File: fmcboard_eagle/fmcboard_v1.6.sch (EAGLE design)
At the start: 235 parts, among them IC1 OPA699ID, IC10 LM358, IC11 7805DT, IC12 SN74AUC2G66DCTR, IC13 SN74AUC2G66DCTR, IC14 SN74AUC2G66DCTR, IC15 SN74AUC2G66DCTR, IC16 DAC7578SPWR, IC17 SN74AUC2G66DCTR, IC18 SN74AUC2G66DCTR, IC19 SN74AUC2G66DCTR, IC2 DAC7578SPWR, IC20 SN74AUC2G66DCTR, IC21 74AUP2GU04GW, IC22 74AUP2GU04GW, IC23 74AUP2GU04GW, IC24 74AUP2GU04GW, IC25 MC7905ACD2TR4G, IC26 AMS1117-1.8, IC29 LM337KVURG3, IC3 LTC6229IMS8E#TRPBF, IC4 OPA695IDR, IC5 LTC6229IMS8E#TRPBF, IC6 OPA695IDR, IC7 OPA699ID, IC8 LM358, IC9 LM358, J1 8pin, J10 4p-2.54, J11 4p-2.54, J12 4p-2.54, J13 4p-2.54, J2 ASP-134604-01, J3 4p-2.54, J4 4p-2.54, J5 4p-2.54, J6 4p-2.54, J7 4p-2.54, J8 4p-2.54, J9 8pin

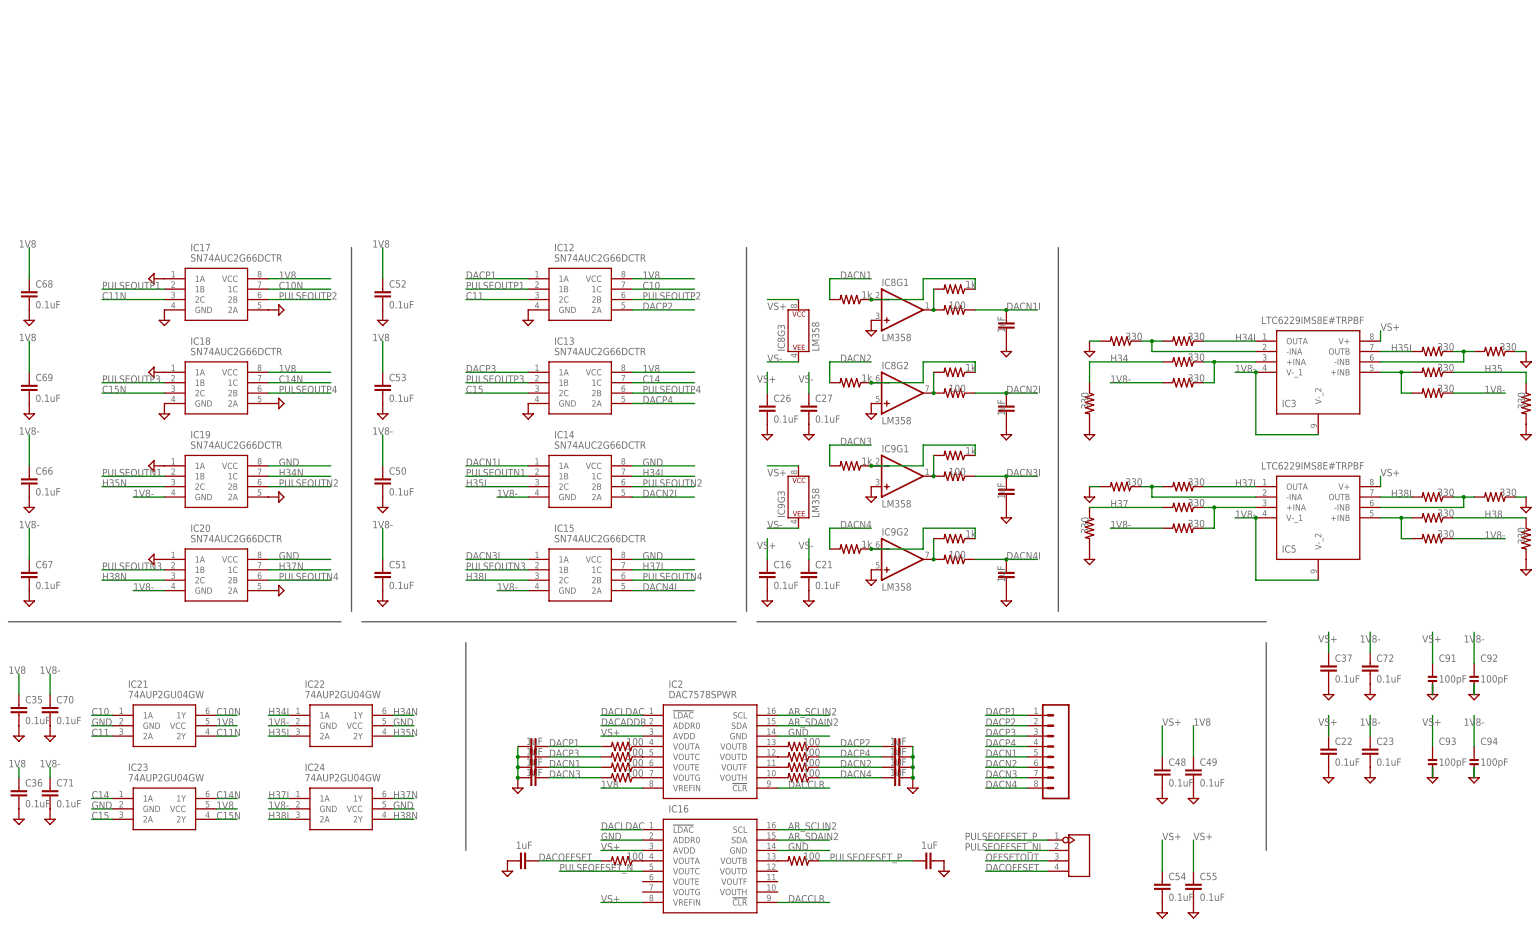
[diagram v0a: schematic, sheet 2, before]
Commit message: Added extra 4 DAC outputs, 2 positive and 2 negative Copies of pulse out and amp out to sma - TODO
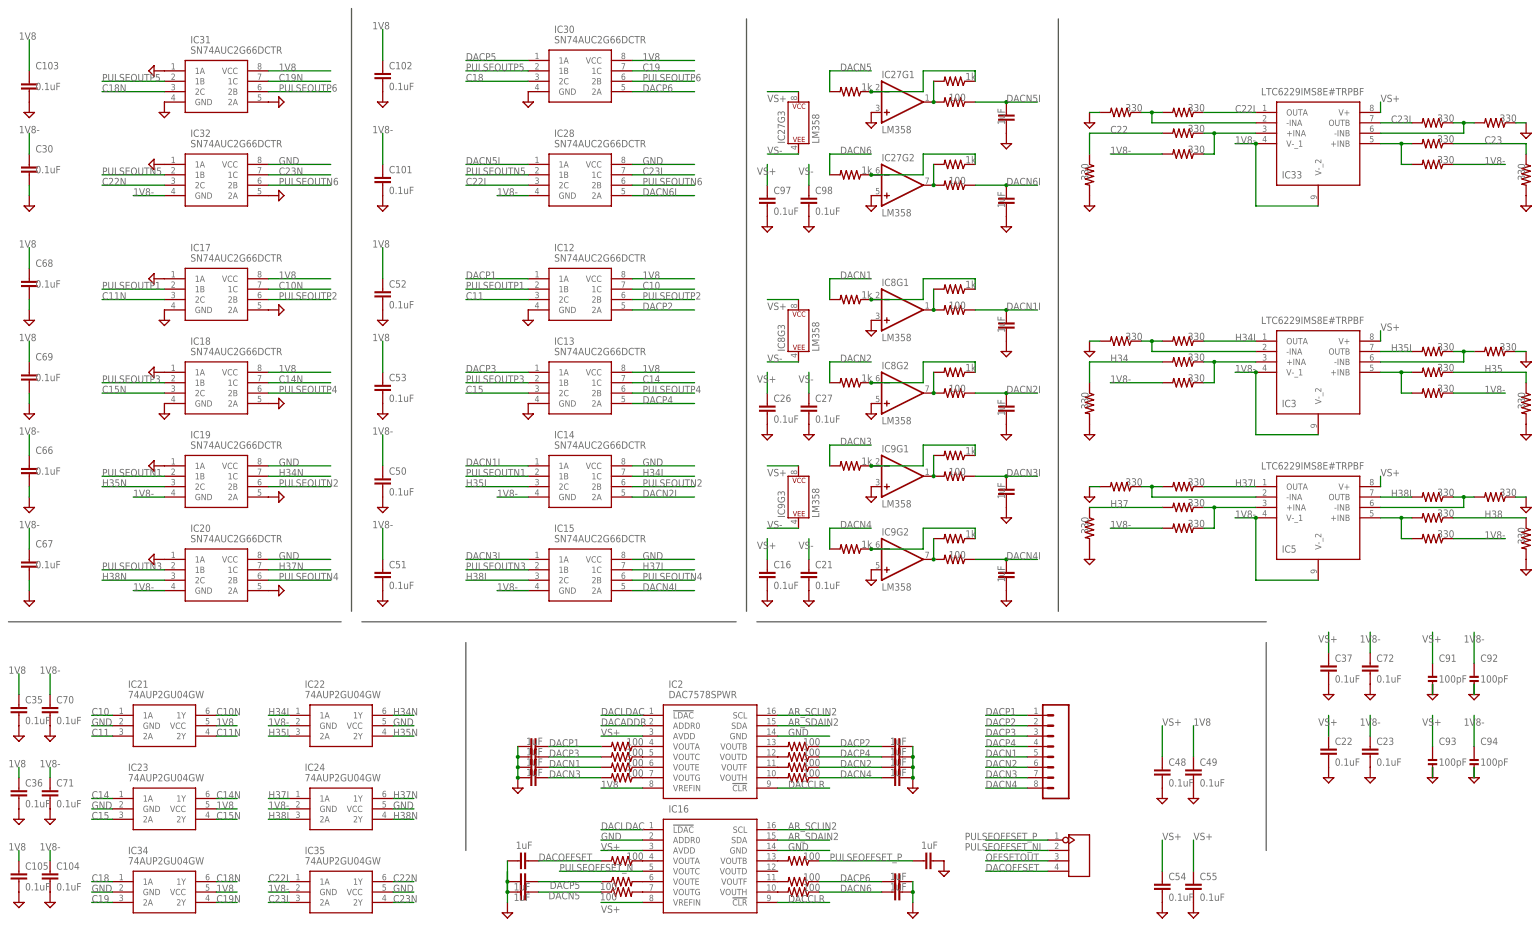
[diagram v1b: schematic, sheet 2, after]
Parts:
- removed J10: 4p-2.54, Seeed-Connector:DIP-BLACK-FEMALE-HEADER-VERT(4P-2.54)
- added C100, C31, C89, C90, C96, C99: 1uF, SparkFun-Passives:CAP0805
- added C101, C102, C104, C105, C97, C98: 0.1uF, SparkFun-Passives:CAP0805
- added C103, C30: 0.1uF, rcl:C-EUC0402K
- added IC27: LM358, SparkFun-IC-Amplifiers:OPAMP-DUALU
- added IC28, IC30, IC31, IC32: SN74AUC2G66DCTR, SN74AUC2G66DCTR:SN74AUC2G66DCTR
- added IC33: LTC6229IMS8E#TRPBF, LTC6229IMS8E#TRPBF:LTC6229IMS8E#TRPBF
- added IC34, IC35: 74AUP2GU04GW, 74AUP2GU04GW_125:74AUP2GU04GW,125
- added R100, R101, R92, R93, R94, R95: 100, rcl:R-US_R0402
- added R102, R103, R104, R105, R106, R107, R108, R109, R110, R91: 330, rcl:R-US_R0402
- added R111, R112, R113, R114: 470, rcl:R-US_R0402
- added R96, R97, R98, R99: 1k, rcl:R-US_R0402
- C66, C67, C68, C69: device SparkFun-Passives:CAP0805 -> rcl:C-EUC0402K
- R1, R10, R11, R12, R13, R14, R17, R18, R19, R2, R20, R21, R22, R23, R24, R25, R26, R27, R28, R29, R3, R30, R31, R32, R33, R34, R35, R36, R37, R38, R39, R40, R41, R42, R43, R44, R45, R46, R47, R48, R49, R50, R51, R52, R53, R54, R55, R56, R57, R58, R59, R6, R60, R61, R62, R63, R64, R65, R66, R67, R68, R69, R7, R70, R73, R74, R75, R76, R77, R78, R79, R8, R80, R81, R82, R83, R84, R85, R87, R88, R90: device rcl:R-US_R0805 -> rcl:R-US_R0402
- R15, R16, R4, R5: device SparkFun-Resistors:RESISTORAXIAL-0.3 -> rcl:R-US_R0402
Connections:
- new net C18N: IC31.2C, IC34.1Y
- new net C19N: IC31.1C, IC34.2Y
- new net C22I: IC28.2C, IC33.OUTA, IC35.1A, R103.1
- new net C22N: IC32.2C, IC35.1Y
- new net C23I: IC28.1C, IC33.OUTB, IC35.2A, R107.2
- new net C23N: IC32.1C, IC35.2Y
- new net DACN5: C96.1, R95.1, R98.2
- new net DACN5I: C99.2, IC28.1A, R100.1
- new net DACN6: C89.1, R93.1, R99.2
- new net DACN6I: C100.2, IC28.2A, R101.1
- new net DACP5: C90.1, IC30.1A, R94.1
- new net DACP6: C31.1, IC30.2A, R92.1
- new net N$1: IC33.-INA, R103.2, R104.1
- new net N$18: IC16.VOUTF, R92.2
- new net N$41: IC16.VOUTH, R93.2
- new net N$43: IC16.VOUTE, R94.2
- new net N$44: IC16.VOUTG, R95.2
- new net N$45: IC27G2.OUT, R101.2, R96.2
- new net N$46: IC27G1.OUT, R100.2, R97.2
- new net N$47: IC27G1.-IN, R97.1, R98.1
- new net N$48: IC27G2.-IN, R96.1, R99.1
- new net N$49: IC33.-INB, R107.1, R108.2
- new net N$50: IC33.+INA, R102.1, R91.1
- new net N$51: IC33.+INB, R105.2, R106.2
- new net PULSEOUTN5: IC28.1B, IC32.1B, R112.2
- new net PULSEOUTN6: IC28.2B, IC32.2B, R114.2
- new net PULSEOUTP5: IC30.1B, IC31.1B, R111.2
- new net PULSEOUTP6: IC30.2B, IC31.2B, R113.2
- net 1V8: now also C102.1, C103.1, C105.1, IC30.VCC, IC31.VCC, IC34.VCC
- net 1V8-: now also C101.1, C104.1, C30.1, IC28.GND, IC32.GND, IC33.V-_1, IC33.V-_2, IC35.GND, R102.2, R106.1
- net C18: now also IC30.2C, IC34.1A; no longer J10.P$1
- net C19: now also IC30.1C, IC34.2A; no longer J10.P$2
- net C22: now also R109.1, R91.2; no longer J10.P$3
- net C23: now also R105.1, R110.1; no longer J10.P$4
- net GND: now also C100.1, C101.2, C102.2, C103.2, C104.2, C105.2, C30.2, C31.2, C89.2, C90.2, C96.2, C97.2, C98.2, C99.1, IC27G1.+IN, IC27G2.+IN, IC28.VCC, IC30.GND, IC31.1A, IC31.2A, IC31.GND, IC32.1A, IC32.2A, IC32.VCC, IC34.GND, IC35.VCC, R104.2, R108.1, R109.2, R110.2
- net PULSESUMIN: now also R111.1, R112.1, R113.1, R114.1
- net VS+: now also C97.1, IC27G3.P$V+, IC33.V+
- net VS-: now also C98.1, IC27G3.P$V-
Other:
- note removed: "extra"
- moved on the sheet: C66, C67, C68, C69

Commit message: Added extra 4 DAC outputs, 2 positive and 2 negative Move to 0402 R and C Copies of pulse out and amp out to sma - TODO
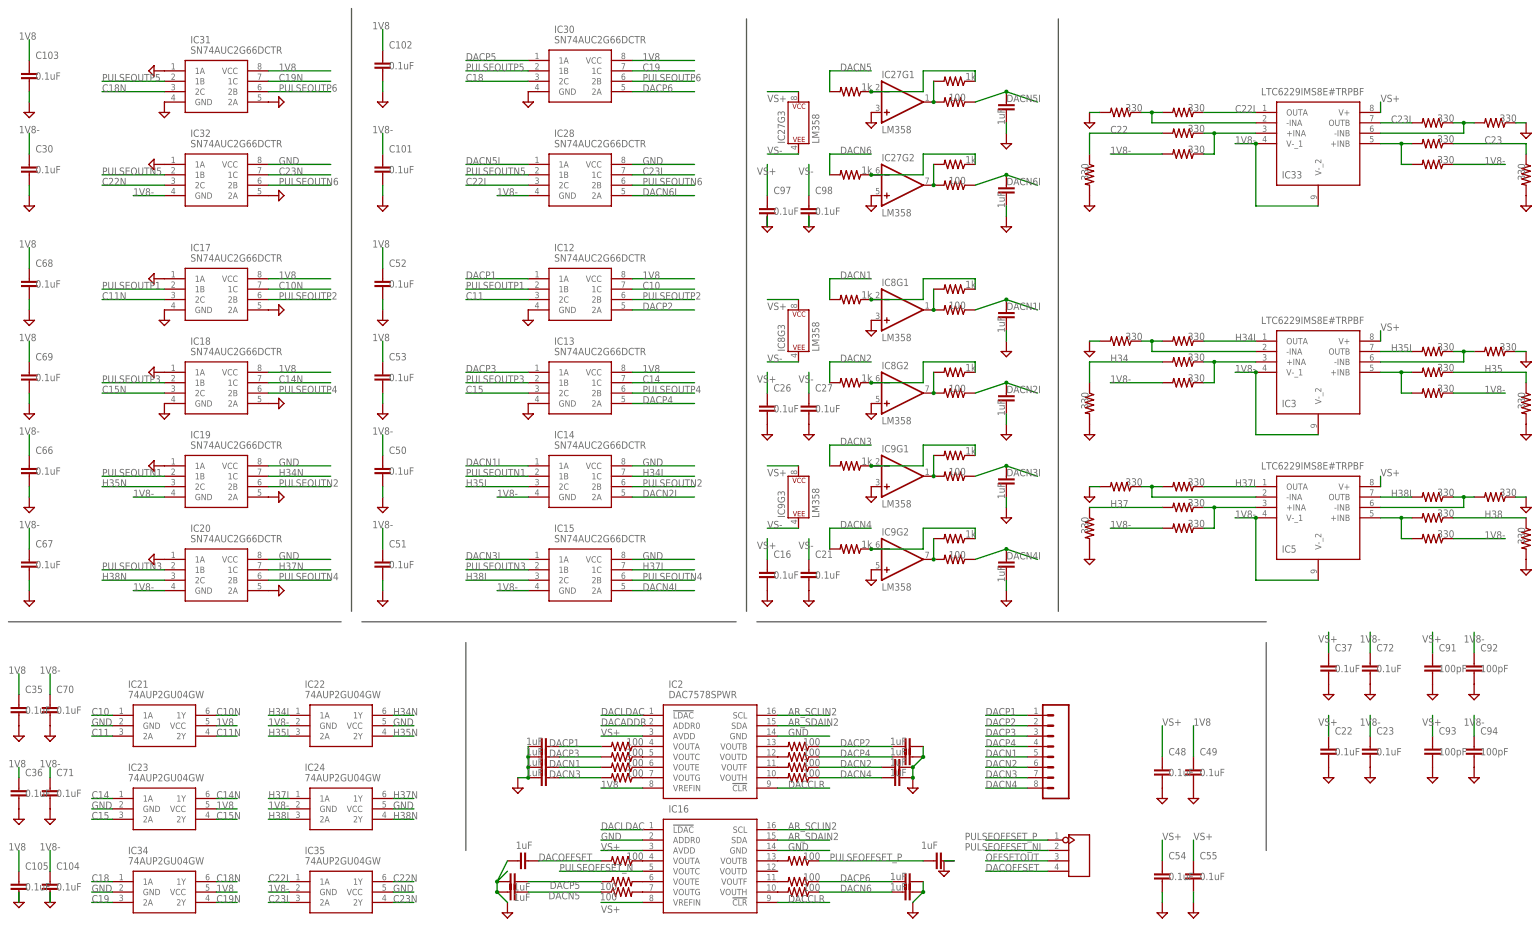
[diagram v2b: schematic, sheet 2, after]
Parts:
- C1, C10, C100, C101, C102, C104, C105, C11, C12, C13, C14, C15, C16, C17, C18, C19, C2, C20, C21, C22, C23, C24, C25, C26, C27, C28, C29, C3, C31, C33, C34, C35, C36, C37, C38, C39, C40, C41, C42, C43, C44, C45, C46, C47, C48, C49, C5, C50, C51, C52, C53, C54, C55, C56, C57, C58, C59, C6, C62, C63, C65, C7, C70, C71, C72, C73, C74, C75, C76, C77, C78, C79, C8, C80, C86, C89, C9, C90, C96, C97, C98, C99: device SparkFun-Passives:CAP0805 -> rcl:C-EUC0402K
- C32, C81, C82, C83, C84, C85, C87, C88, C91, C92, C93, C94: device passives:CAPACITOR0603_CAP -> rcl:C-EUC0402K
- R71, R72, R86, R89: device rcl:R-US_R0805 -> rcl:R-US_R0402
- R9: device SparkFun-Resistors:RESISTORAXIAL-0.3 -> resistor:R-US_R0805
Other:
- moved on the sheet: C101, C102, C103, C104, C105, C50, C51, C52, C53, C54, C55, C97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

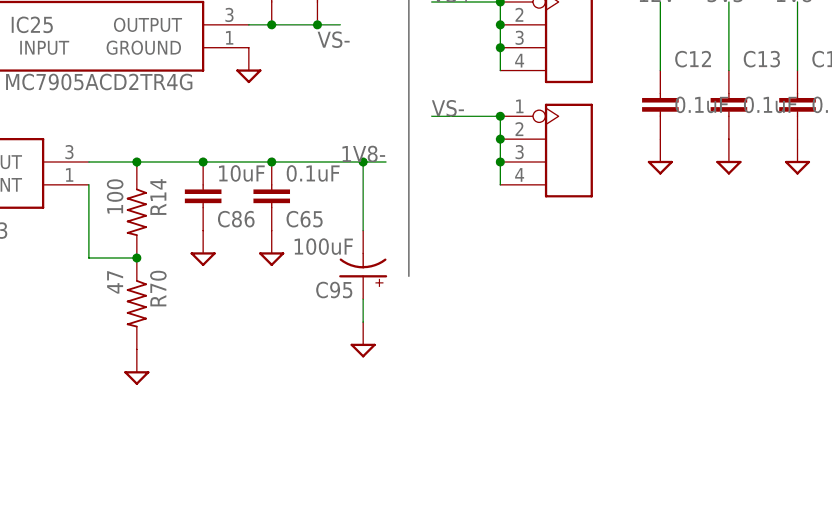
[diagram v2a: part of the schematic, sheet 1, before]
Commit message: Added extra 4 DAC outputs, 2 positive and 2 negative Move all to 0402 R and C Replace 100uF with 10 10uF Copies of pulse out and amp out to sma - TODO
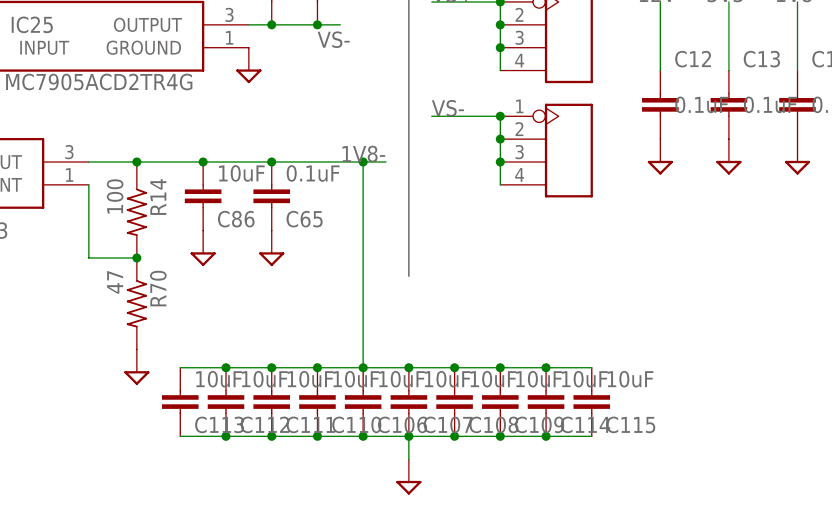
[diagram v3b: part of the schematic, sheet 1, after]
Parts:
- removed C95: 100uF, SparkFun-Passives:CAP_POLSMD
- added C106, C107, C108, C109, C110, C111, C112, C113, C114, C115: 10uF, rcl:C-EUC0402K
- C4, C60, C61, C64: device SparkFun-Passives:CAP0805 -> rcl:C-EUC0402K
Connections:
- net 1V8-: now also C106.1, C107.1, C108.1, C109.1, C110.1, C111.1, C112.1, C113.1, C114.1, C115.1; no longer C95.-
- net GND: now also C106.2, C107.2, C108.2, C109.2, C110.2, C111.2, C112.2, C113.2, C114.2, C115.2; no longer C95.+
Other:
- moved on the sheet: C104, C105, C97, C98

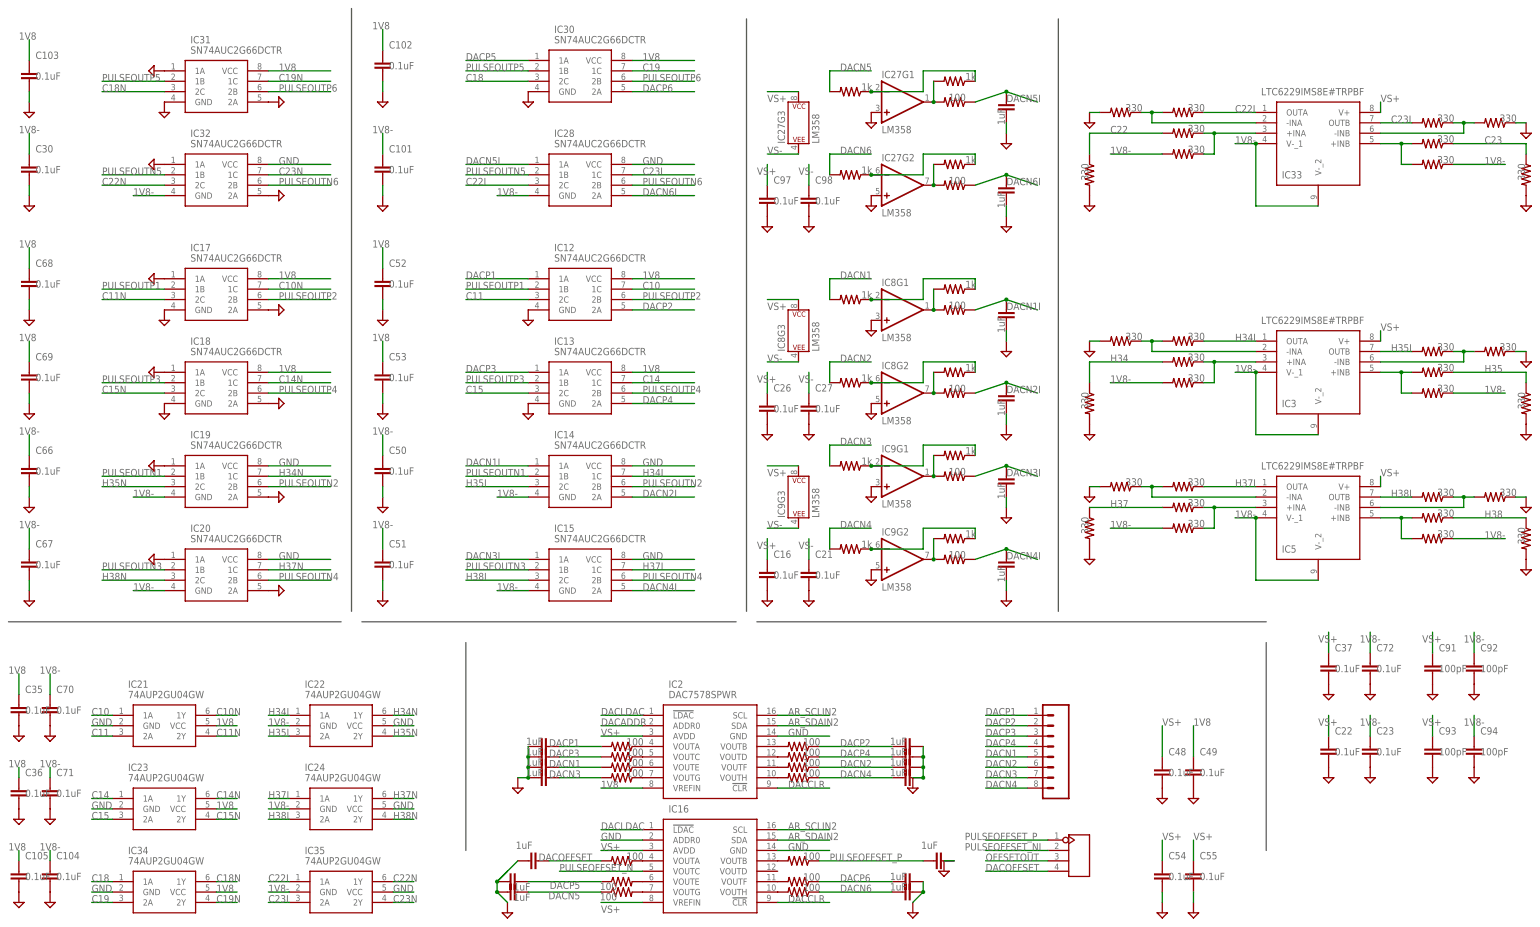
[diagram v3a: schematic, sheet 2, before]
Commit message: Added extra 4 DAC outputs, 2 positive and 2 negative Move all to 0402 R and C Replace 100uF with 10 10uF Remove dacoffset variable resistor, replace with DAC N Set VH and VL to 1.8 and GND Copies of pulse out and amp out to sma - TODO
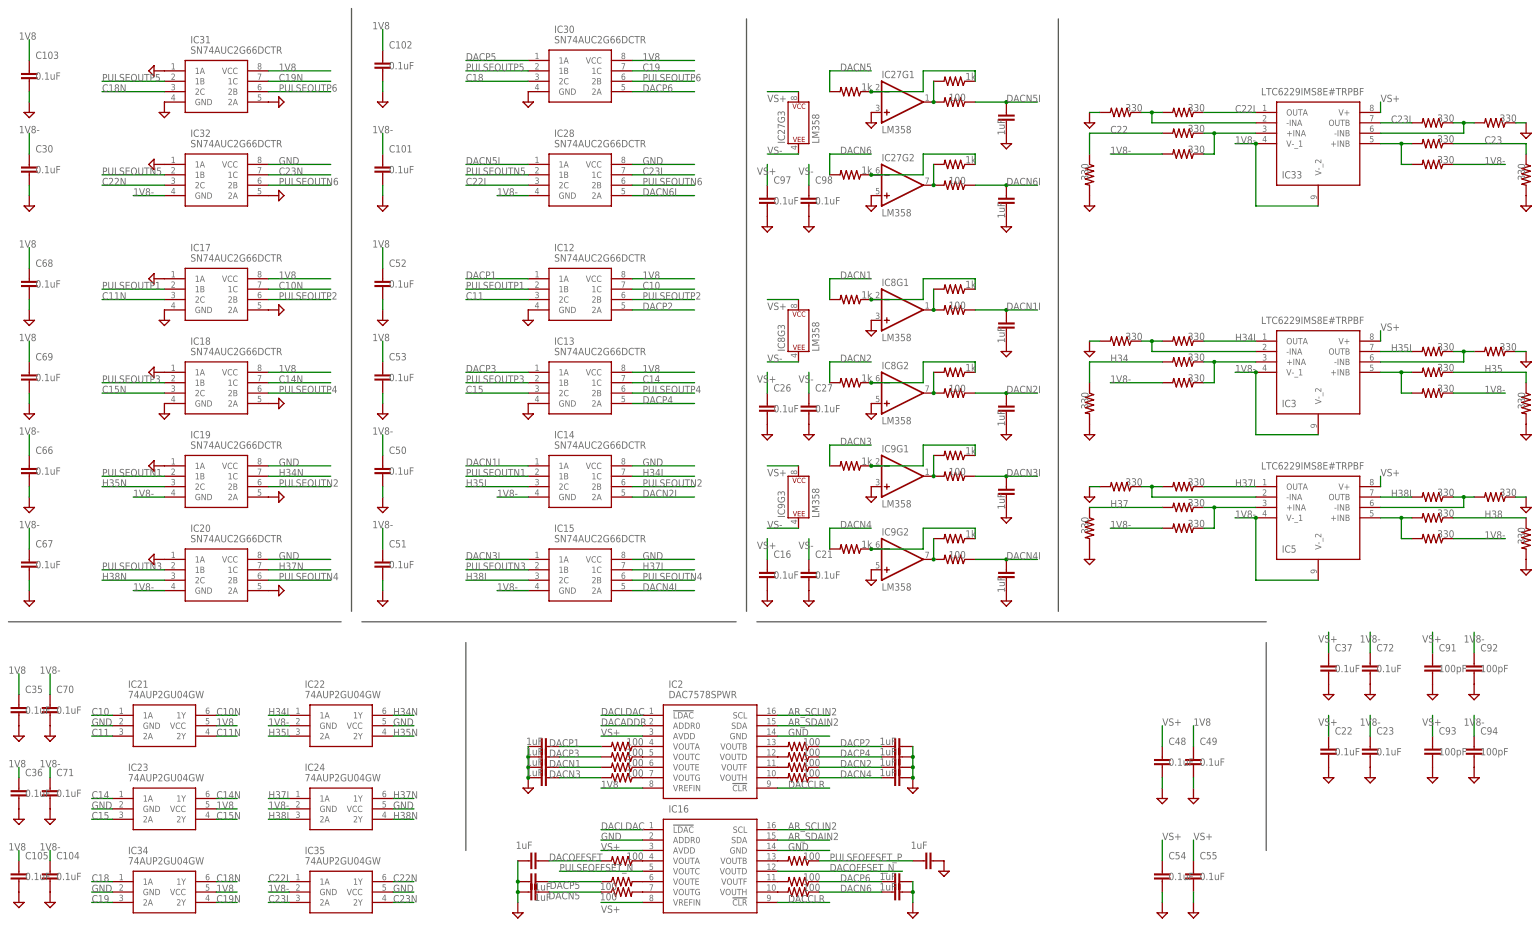
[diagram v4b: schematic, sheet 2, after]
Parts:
- removed C4: 0.1uF, rcl:C-EUC0402K
- removed J11: 4p-2.54, Seeed-Connector:DIP-BLACK-FEMALE-HEADER-VERT(4P-2.54)
- removed J9: 8pin, SparkFun-Connectors:CONN_08"
- removed R_O2, R_VH, R_VL: 5k, resistor:R-TRIMM3296W
- added R115: 1k, rcl:R-US_R0402
- R17: value 4.7k -> 1k
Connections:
- removed net OFFSETIN: C4.1, IC10G2.+IN, R17.1
- removed net OFFSETOUT: IC10G2.-IN, IC10G2.OUT, J11.P$3, R25.2
- removed net VH: C7.1, IC7.VH, J1.3, R_VH.S
- removed net VL: C8.1, IC7.VL, J1.4, R_VL.S
- new net DACOFFSETOUT_N: IC10G2.OUT, R115.2, R25.2
- new net DACOFFSET_N: IC16.VOUTD, R17.2
- net 1V8: now also C7.1, IC7.VH
- net DACN1: no longer J9.5
- net DACN2: no longer J9.6
- net DACN3: no longer J9.7
- net DACN4: no longer J9.8
- net DACOFFSET: no longer J11.P$4
- net DACP1: no longer J9.1
- net DACP2: no longer J9.2
- net DACP3: no longer J9.3
- net DACP4: no longer J9.4
- net GND: now also C8.1, IC10G2.+IN, IC7.VL, J1.3, J1.4; no longer C4.2, R_VH.A, R_VL.A
- net N$2: now also IC10G2.-IN, R115.1, R17.1; no longer R17.2, R_O2.S
- net PULSEOFFSET_NI: no longer J11.P$2
- net PULSEOFFSET_P: no longer J11.P$1
- net VS+: no longer R_O2.E, R_VH.E
- net VS-: no longer R_O2.A, R_VL.E
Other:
- note added: "10*10uF=100uF"
- moved on the sheet: C28, C29, C32, C48, C49, C78, C79, C81, C87, C88
